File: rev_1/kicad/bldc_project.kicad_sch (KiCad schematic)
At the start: 0 parts

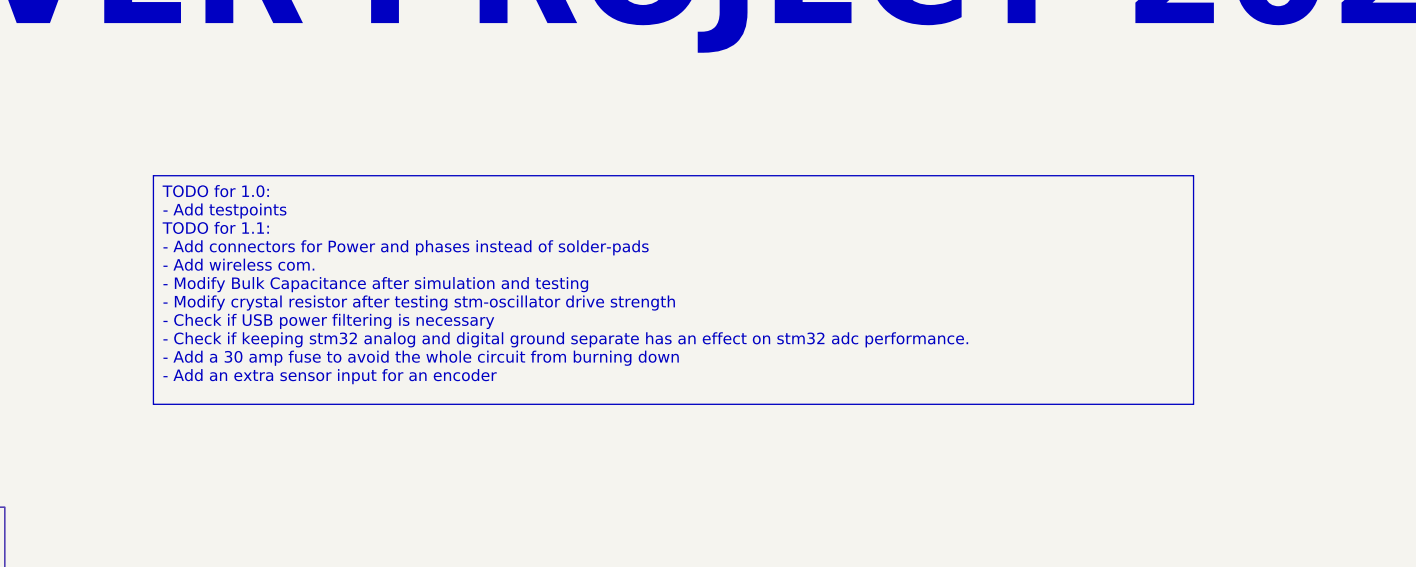
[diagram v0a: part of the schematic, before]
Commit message: [kicad] (minor) Added comments about bldc strategy
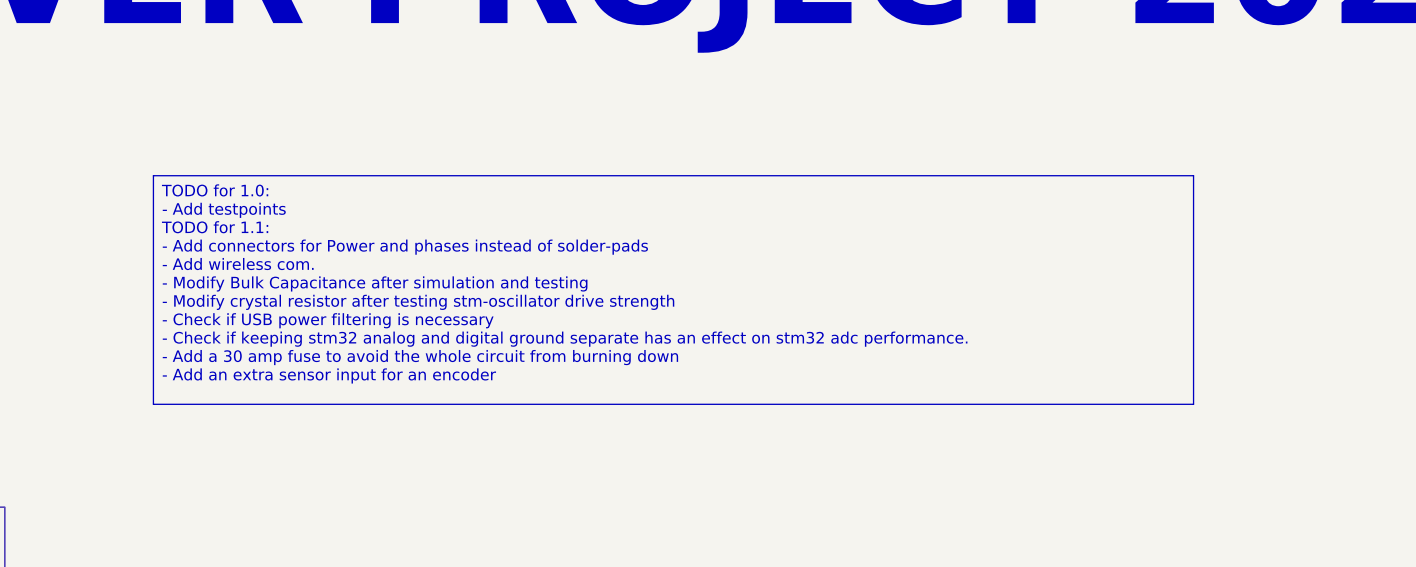
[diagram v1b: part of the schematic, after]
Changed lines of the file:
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@@
 (kicad_sch
-	(version 20231120)
+	(version 20250114)
 	(generator "eeschema")
-	(generator_version "8.0")
+	(generator_version "9.0")
 	(paper "A4")
 	(title_block
@@
 		(company "IW")
 	)
+	(text "BLDC DRIVER PROJECT 2024"
+		(exclude_from_sim no)
+		(at 17.78 34.29 0)
+		(effects
+			(font
+				(size 12 12)
+				(thickness 2.4)
+				(bold yes)
+			)
+			(justify left bottom)
+		)
+	)
 	(text_box "TODO for 1.0:\n- Add testpoints\nTODO for 1.1:\n- Add connectors for Power and phases instead of solder-pads\n- Add wireless com.\n- Modify Bulk Capacitance after simulation and testing\n- Modify crystal resistor after testing stm-oscillator drive strength\n- Check if USB power filtering is necessary\n- Check if keeping stm32 analog and digital ground separate has an effect on stm32 adc performance.\n- Add a 30 amp fuse to avoid the whole circuit from burning down\n- Add an extra sensor input for an encoder"
 		(exclude_from_sim no)
 		(at 124.46 49.53 0)
 		(size 115.57 25.4)
+		(margins 0.9525 0.9525 0.9525 0.9525)
 		(stroke
 			(width 0)
@@
 		)
 	)
-	(text "BLDC DRIVER PROJECT 2024"
-		(exclude_from_sim no)
-		(at 17.78 34.29 0)
-		(effects
-			(font
-				(size 12 12)
-				(thickness 2.4)
-				(bold yes)
-			)
-			(justify left bottom)
-		)
-	)
 	(sheet
 		(at 22.86 127)
 		(size 86.36 26.67)
+		(exclude_from_sim no)
+		(in_bom yes)
+		(on_board yes)
+		(dnp no)
 		(fields_autoplaced yes)
 		(stroke
@@
 		(at 22.86 86.36)
 		(size 85.09 26.67)
+		(exclude_from_sim no)
+		(in_bom yes)
+		(on_board yes)
+		(dnp no)
 		(fields_autoplaced yes)
 		(stroke
@@
 		(at 22.86 50.8)
 		(size 74.93 24.13)
+		(exclude_from_sim no)
+		(in_bom yes)
+		(on_board yes)
+		(dnp no)
 		(fields_autoplaced yes)
 		(stroke
@@
 		)
 	)
+	(embedded_fonts no)
 )
